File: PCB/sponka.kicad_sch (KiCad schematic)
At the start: 3 parts, among them J1 Conn_01x03_Pin, U1 CH32V003FxUx

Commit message: Made first PCB
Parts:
- added C5: 100nF, Capacitor_SMD:C_0402_1005Metric, symbol Device:C_Small
- added SW2: SW_Push, Button_Switch_SMD:SW_SPST_B3U-1000P-B, symbol Switch:SW_Push
- C1: footprint Capacitor_SMD:C_0504_1310Metric -> Capacitor_SMD:C_0402_1005Metric
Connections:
- net GND: now also C5.1, SW2.2
- net at U1.1 (PD7): now also C5.2, SW2.1
- net Power management/USB_DN: now reaches U1.17 (PD3)
- net Power management/USB_DP: now reaches U1.18 (PD4)
- net Power management/BATT_DIV: now reaches U1.19 (PD5)
- net LEDRow0 renamed LED Row/Row_DIN
- net LEDRow1: no longer names the net of U1.8 (PC1)
- net LEDRow2: no longer names the net of U1.9 (PC2)
- net LEDRow3: no longer names the net of U1.10 (PC3)
- net LEDRow4: no longer names the net of U1.11 (PC4)
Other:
- removed sheet LED Row1
- removed sheet LED Row2
- removed sheet LED Row3
- removed sheet LED Row4
- sheet Power management ports: added +3V3, BATT_DIV, GND, USB_DN, USB_DP; removed none
- moved on the sheet: J1

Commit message: PCB V2
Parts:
- J1: footprint Connector_PinHeader_2.54mm:PinHeader_1x03_P2.54mm_Vertical -> sponka:pogo_pins
- renumbered C5 to C2, SW2 to SW1
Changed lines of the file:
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@@
 		(dnp no)
 		(fields_autoplaced yes)
-		(property "Reference" "#PWR01"
+		(property "Reference" "#PWR05"
 			(at 185.42 60.96 0)
 			(effects
@@
 			(project ""
 				(path "/cd633adc-49f5-4b4f-8d72-c74316356641"
-					(reference "#PWR01")
+					(reference "#PWR05")
 					(unit 1)
 				)
@@
 		(dnp no)
 		(fields_autoplaced yes)
-		(property "Reference" "#PWR02"
+		(property "Reference" "#PWR06"
 			(at 185.42 77.47 0)
 			(effects
@@
 			(project ""
 				(path "/cd633adc-49f5-4b4f-8d72-c74316356641"
-					(reference "#PWR02")
+					(reference "#PWR06")
 					(unit 1)
 				)
@@
 		(dnp no)
 		(fields_autoplaced yes)
-		(property "Reference" "#PWR014"
+		(property "Reference" "#PWR02"
 			(at 144.78 114.3 0)
 			(effects
@@
 			(project "sponka"
 				(path "/cd633adc-49f5-4b4f-8d72-c74316356641"
-					(reference "#PWR014")
+					(reference "#PWR02")
 					(unit 1)
 				)
@@
 		(dnp no)
 		(fields_autoplaced yes)
-		(property "Reference" "#PWR022"
+		(property "Reference" "#PWR07"
 			(at 191.77 116.84 0)
 			(effects
@@
 			(project ""
 				(path "/cd633adc-49f5-4b4f-8d72-c74316356641"
-					(reference "#PWR022")
+					(reference "#PWR07")
 					(unit 1)
 				)
@@
 		(dnp no)
 		(fields_autoplaced yes)
-		(property "Reference" "#PWR015"
+		(property "Reference" "#PWR01"
 			(at 130.81 64.77 0)
 			(effects
@@
 			(project "sponka"
 				(path "/cd633adc-49f5-4b4f-8d72-c74316356641"
-					(reference "#PWR015")
+					(reference "#PWR01")
 					(unit 1)
 				)
@@
 		(on_board yes)
 		(dnp no)
-		(property "Reference" "C5"
+		(property "Reference" "C2"
 			(at 173.99 126.746 90)
 			(effects
@@
 			(project "sponka"
 				(path "/cd633adc-49f5-4b4f-8d72-c74316356641"
-					(reference "C5")
+					(reference "C2")
 					(unit 1)
 				)
@@
 		(dnp no)
 		(fields_autoplaced yes)
-		(property "Reference" "SW2"
+		(property "Reference" "SW1"
 			(at 173.99 109.22 0)
 			(effects
@@
 			(project ""
 				(path "/cd633adc-49f5-4b4f-8d72-c74316356641"
-					(reference "SW2")
+					(reference "SW1")
 					(unit 1)
 				)
@@
 		(dnp no)
 		(fields_autoplaced yes)
-		(property "Reference" "#PWR013"
+		(property "Reference" "#PWR03"
 			(at 143.51 64.77 0)
 			(effects
@@
 			(project "sponka"
 				(path "/cd633adc-49f5-4b4f-8d72-c74316356641"
-					(reference "#PWR013")
+					(reference "#PWR03")
 					(unit 1)
 				)
@@
 			)
 		)
-		(property "Footprint" "Connector_PinHeader_2.54mm:PinHeader_1x03_P2.54mm_Vertical"
+		(property "Footprint" "sponka:pogo_pins"
 			(at 194.31 64.77 0)
 			(effects
@@
 		(dnp no)
 		(fields_autoplaced yes)
-		(property "Reference" "#PWR020"
+		(property "Reference" "#PWR04"
 			(at 175.26 92.71 0)
 			(effects
@@
 			(project "sponka"
 				(path "/cd633adc-49f5-4b4f-8d72-c74316356641"
-					(reference "#PWR020")
-					(unit 1)
-				)
+					(reference "#PWR04")
+					(unit 1)
+				)

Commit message: Probably the final update
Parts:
- added J4: Conn_01x05_Pin, sponka:pogo_pins_1_5, symbol Connector:Conn_01x05_Pin
- added R9: 5,1k, Resistor_SMD:R_0402_1005Metric, symbol Device:R_Small
- J1: footprint sponka:pogo_pins -> sponka:pogo_pins_1_3
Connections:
- net +3V3: now also J4.1 (Pin_1)
- net GND: now also J4.5 (Pin_5)
- net LED Row/Row_DIN: now also U1.13 (PC6); no longer U1.7 (PC0)
- net Power management/USB_DN: now also R9.2
- net DPU: now reaches U1.16 (PD2)
- net DPU: now also R9.1
- net RX/SDA: now reaches U1.8 (PC1)
- net RX/SDA: now also J4.3 (Pin_3)
- net RTS/SCL: now reaches U1.9 (PC2)
- net RTS/SCL: now also J4.4 (Pin_4)
- new net TX: J4.2 (Pin_2), U1.7 (PC0)

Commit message: Progress update
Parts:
- SW1: footprint Button_Switch_SMD:SW_SPST_B3U-1000P-B -> Button_Switch_SMD:SW_SPST_B3U-1000P
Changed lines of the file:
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@@
 			)
 		)
-		(property "Footprint" "Button_Switch_SMD:SW_SPST_B3U-1000P-B"
+		(property "Footprint" "Button_Switch_SMD:SW_SPST_B3U-1000P"
 			(at 173.99 111.76 0)
 			(effects

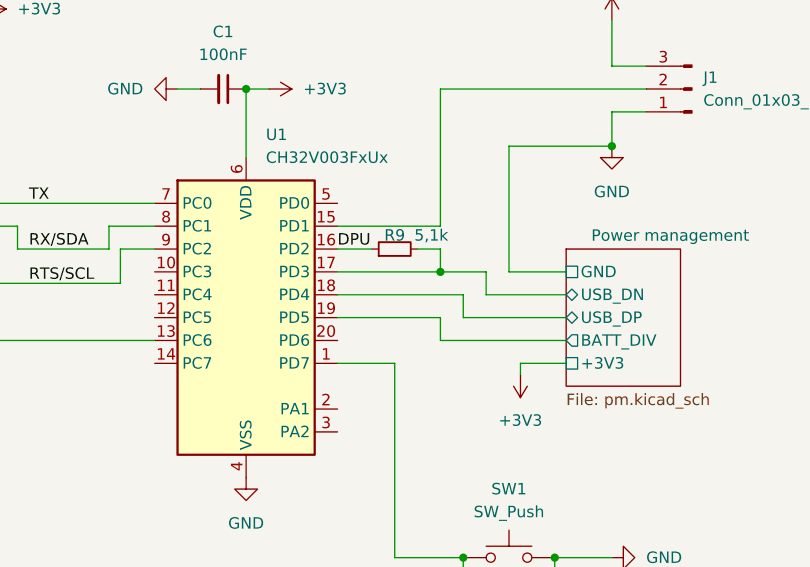
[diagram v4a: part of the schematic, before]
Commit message: Add USBLC6-2P6 for ESD protection The usual COMPLETE REDESIGN because it didn't fit
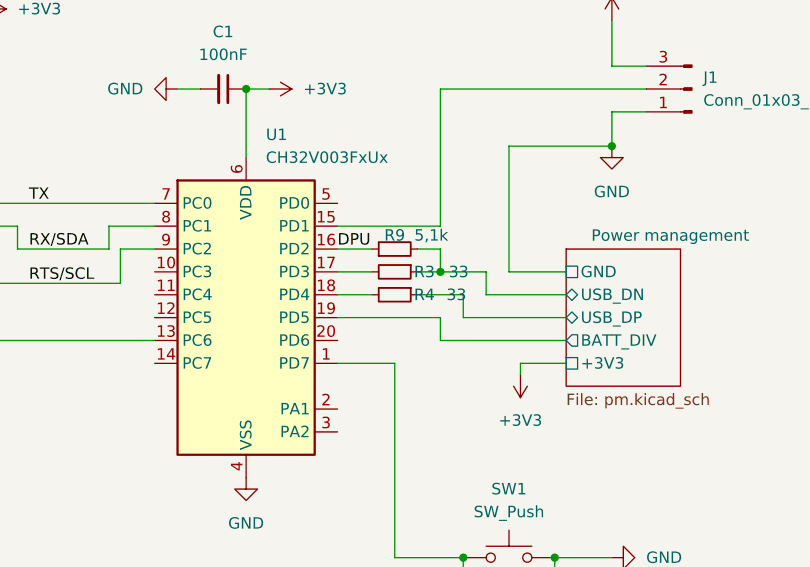
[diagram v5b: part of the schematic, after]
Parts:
- added R3, R4: 33, Resistor_SMD:R_0402_1005Metric, symbol Device:R_Small
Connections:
- net Power management/USB_DN: now also R3.1; no longer U1.17 (PD3)
- net Power management/USB_DP: now also R4.1; no longer U1.18 (PD4)
- new net: R3.2, U1.17 (PD3)
- new net: R4.2, U1.18 (PD4)
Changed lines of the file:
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@@
 	(wire
 		(pts
-			(xy 168.91 87.63) (xy 154.94 87.63)
+			(xy 168.91 87.63) (xy 163.83 87.63)
 		)
 		(stroke
@@
 	(wire
 		(pts
+			(xy 158.75 87.63) (xy 154.94 87.63)
+		)
+		(stroke
+			(width 0)
+			(type default)
+		)
+	)
+	(wire
+		(pts
 			(xy 105.41 53.34) (xy 105.41 86.36)
 		)
@@
 	(wire
 		(pts
-			(xy 166.37 85.09) (xy 154.94 85.09)
+			(xy 166.37 85.09) (xy 163.83 85.09)
 		)
 		(stroke
@@
 		(pts
 			(xy 99.06 55.88) (xy 102.87 55.88)
+		)
+		(stroke
+			(width 0)
+			(type default)
+		)
+	)
+	(wire
+		(pts
+			(xy 158.75 85.09) (xy 154.94 85.09)
 		)
 		(stroke
@@
 	)
 	(symbol
+		(lib_id "Device:R_Small")
+		(at 161.29 85.09 270)
+		(unit 1)
+		(exclude_from_sim no)
+		(in_bom yes)
+		(on_board yes)
+		(dnp no)
+		(property "Reference" "R3"
+			(at 164.592 85.09 90)
+			(effects
+				(font
+					(size 1.27 1.27)
+				)
+			)
+		)
+		(property "Value" "33"
+			(at 168.402 85.09 90)
+			(effects
+				(font
+					(size 1.27 1.27)
+				)
+			)
+		)
+		(property "Footprint" "Resistor_SMD:R_0402_1005Metric"
+			(at 161.29 85.09 0)
+			(effects
+				(font
+					(size 1.27 1.27)
+				)
+				(hide yes)
+			)
+		)
+		(property "Datasheet" "~"
+			(at 161.29 85.09 0)
+			(effects
+				(font
+					(size 1.27 1.27)
+				)
+				(hide yes)
+			)
+		)
+		(property "Description" "Resistor, small symbol"
+			(at 161.29 85.09 0)
+			(effects
+				(font
+					(size 1.27 1.27)
+				)
+				(hide yes)
+			)
+		)
+		(pin "1"
+		)
+		(pin "2"
+		)
+		(instances
+			(project "sponka"
+				(path "/cd633adc-49f5-4b4f-8d72-c74316356641"
+					(reference "R3")
+					(unit 1)
+				)
+			)
+		)
+	)
+	(symbol
 		(lib_id "Device:C_Small")
 		(at 142.24 64.77 270)
@@
 					(unit 1)
 				)
+			)
+		)
+	)
+	(symbol
+		(lib_id "Device:R_Small")
+		(at 161.29 87.63 270)
+		(unit 1)
+		(exclude_from_sim no)
+		(in_bom yes)
+		(on_board yes)
+		(dnp no)
+		(property "Reference" "R4"
+			(at 164.592 87.63 90)
+			(effects
+				(font
+					(size 1.27 1.27)
+				)
+			)
+		)
+		(property "Value" "33"
+			(at 168.148 87.63 90)
+			(effects
+				(font
+					(size 1.27 1.27)
+				)
+			)
+		)
+		(property "Footprint" "Resistor_SMD:R_0402_1005Metric"
+			(at 161.29 87.63 0)
+			(effects
+				(font
+					(size 1.27 1.27)
+				)
+				(hide yes)
+			)
+		)
+		(property "Datasheet" "~"
+			(at 161.29 87.63 0)
+			(effects
+				(font
+					(size 1.27 1.27)
+				)
+				(hide yes)
+			)
+		)
+		(property "Description" "Resistor, small symbol"
+			(at 161.29 87.63 0)
+			(effects
+				(font
+					(size 1.27 1.27)
+				)
+				(hide yes)
+			)
+		)
+		(pin "1"
+		)
+		(pin "2"
+		)
+		(instances
+			(project "sponka"
+				(path "/cd633adc-49f5-4b4f-8d72-c74316356641"
+					(reference "R4")
+					(unit 1)
+				)

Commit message: Fix wrong values
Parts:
- R9: value 5,1k -> 1.5k
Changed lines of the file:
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@@
 			)
 		)
-		(property "Value" "5,1k"
+		(property "Value" "1.5k"
 			(at 165.354 81.026 90)
 			(effects
@@
 		(dnp no)
 		(property "Reference" "R3"
-			(at 164.592 85.09 90)
+			(at 164.592 83.82 90)
 			(effects
 				(font
@@
 		)
 		(property "Value" "33"
-			(at 168.402 85.09 90)
+			(at 168.148 83.82 90)
 			(effects
 				(font
@@
 		(dnp no)
 		(property "Reference" "R4"
-			(at 164.592 87.63 90)
+			(at 164.592 86.614 90)
 			(effects
 				(font
@@
 		)
 		(property "Value" "33"
-			(at 168.148 87.63 90)
-			(effects
-				(font
+			(at 168.148 86.614 90)
+			(effects
+				(font
